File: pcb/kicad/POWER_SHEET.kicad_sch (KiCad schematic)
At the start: 11 parts, among them J1 USB_B_Micro, U1 LMS1585AIS-3.3

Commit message: Update parts/mpns/descriptions etc.
- Incorrect LED part, was 0805 package instead of 0603
- Added MPNs for other parts (mostly ones I already own multiples of)
- Update schematics?
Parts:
- D1: footprint Diode_SMD:Nexperia_DSN1608-2_1.6x0.8mm -> Diode_SMD:D_SOD-523; MPN (none) -> PESD5V0X1UAB,115
- J1: MPN (none) -> 10118194-0001LF
- R1: MPN (none) -> RT0603DRE071KL
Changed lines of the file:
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@@
+			)
+		)
+		(property "MPN" "10118194-0001LF"
+			(at 68.58 72.39 90)
+			(effects
+				(font
+					(size 1.27 1.27)
+				)
+				(hide yes)
 			)
 		)
@@
 			)
 		)
+		(property "MPN" "RT0603DRE071KL"
+			(at 190.5 62.23 0)
+			(effects
+				(font
+					(size 1.27 1.27)
+				)
+				(hide yes)
+			)
+		)
 		(pin "2"
 		)
@@
 			)
 		)
-		(property "Footprint" "Diode_SMD:Nexperia_DSN1608-2_1.6x0.8mm"
+		(property "Footprint" "Diode_SMD:D_SOD-523"
 			(at 48.895 63.5 0)
 			(effects
@@
 			)
 		)
-		(property "Datasheet" "https://assets.nexperia.com/documents/data-sheet/PTVS5V0Z1USKP.pdf"
+		(property "Datasheet" ""
 			(at 53.34 63.5 0)
 			(effects
@@
 			)
 		)
-		(property "Description" "5V, 2000W TVS unidirectional diode, DSN1608-2"
+		(property "Description" "5V, TVS unidirectional diode"
 			(at 53.34 63.5 0)
 			(effects
 				(font
+					(size 1.27 1.27)
+				)
+				(hide yes)
+			)
+		)
+		(property "MPN" "PESD5V0X1UAB,115"
+			(at 53.34 63.5 90)
+			(effects
+				(font

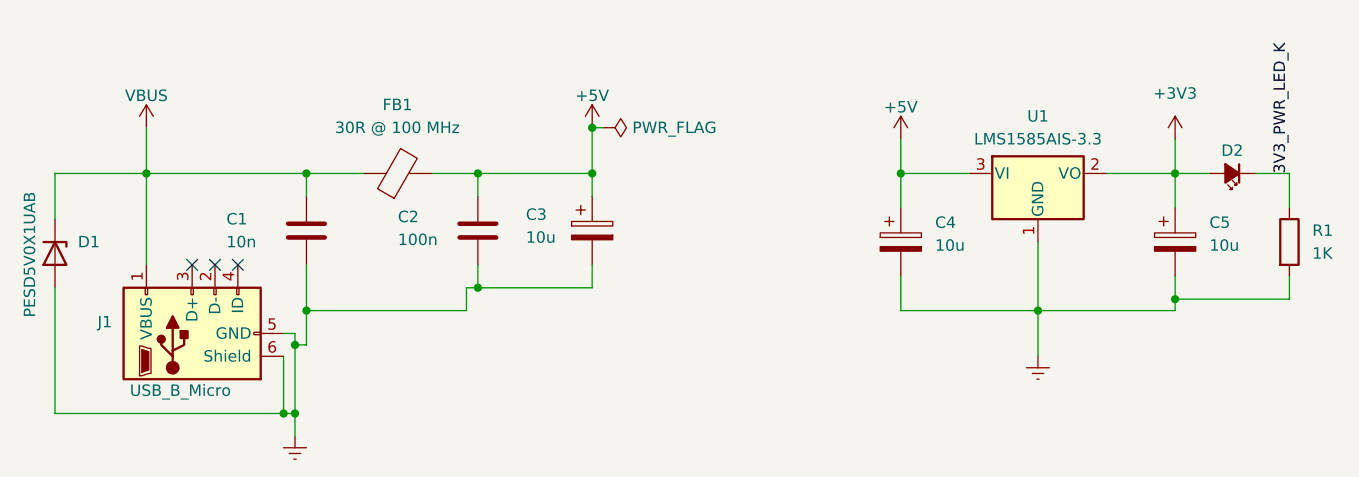
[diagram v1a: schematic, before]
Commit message: Remove additional input cap on ldo
- Already an input capacitor due to the pi-filter on the VBUS line,
  therefore another input capacitor isn't needed
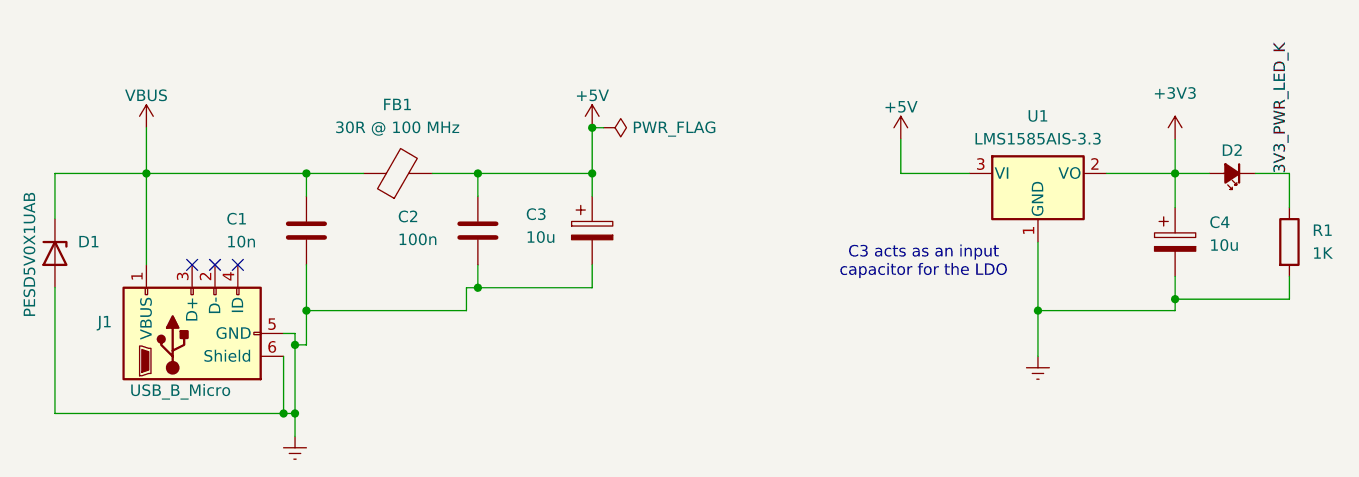
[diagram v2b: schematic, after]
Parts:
- removed C4: 10u, Capacitor_SMD:CP_Elec_4x4.5, symbol Device:C_Polarized
- renumbered C5 to C4
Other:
- note added: "C3 acts as an input capacitor for the LDO"
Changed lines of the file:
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@@
 	(title_block
 		(title "Power Sheet")
-		(date "2025-05-06")
-		(rev "v06")
+		(date "2025-05-21")
+		(rev "v07")
 		(comment 4 "All things power related")
+	)
+	(text "C3 acts as an input \ncapacitor for the LDO"
+		(exclude_from_sim no)
+		(at 149.86 64.516 0)
+		(effects
+			(font
+				(size 1.27 1.27)
+			)
+		)
 	)
 	(junction
@@
 	)
 	(junction
-		(at 147.32 54.61)
-		(diameter 0)
-		(color 0 0 0 0)
-	)
-	(junction
 		(at 80.01 73.66)
 		(diameter 0)
@@
 	(wire
 		(pts
-			(xy 147.32 54.61) (xy 147.32 58.42)
-		)
-		(stroke
-			(width 0)
-			(type default)
-		)
-	)
-	(wire
-		(pts
 			(xy 177.8 66.04) (xy 177.8 68.58)
 		)
@@
 	(wire
 		(pts
-			(xy 147.32 69.85) (xy 162.56 69.85)
-		)
-		(stroke
-			(width 0)
-			(type default)
-		)
-	)
-	(wire
-		(pts
 			(xy 100.33 67.31) (xy 113.03 67.31)
 		)
@@
 		(pts
 			(xy 99.06 69.85) (xy 81.28 69.85)
-		)
-		(stroke
-			(width 0)
-			(type default)
-		)
-	)
-	(wire
-		(pts
-			(xy 147.32 66.04) (xy 147.32 69.85)
 		)
 		(stroke
@@
 		(dnp no)
 		(fields_autoplaced yes)
-		(property "Reference" "C5"
+		(property "Reference" "C4"
 			(at 181.61 60.0709 0)
 			(effects
@@
 			(project "i2s_spekky_matrix"
 				(path "/e164be4c-4870-49b4-a08f-d162a756edc1/8084362c-1e50-4cdc-88cb-8f42b053a44a"
-					(reference "C5")
+					(reference "C4")
 					(unit 1)
 				)
@@
 					(unit 1)
 				)
-			)
-		)
-	)
-	(symbol
-		(lib_id "Device:C_Polarized")
-		(at 147.32 62.23 0)
-		(unit 1)
-		(exclude_from_sim no)
-		(in_bom yes)
-		(on_board yes)
-		(dnp no)
-		(fields_autoplaced yes)
-		(property "Reference" "C4"
-			(at 151.13 60.0709 0)
-			(effects
-				(font
-					(size 1.27 1.27)
-				)
-				(justify left)
-			)
-		)
-		(property "Value" "10u"
-			(at 151.13 62.6109 0)
-			(effects
-				(font
-					(size 1.27 1.27)
-				)
-				(justify left)
-			)
-		)
-		(property "Footprint" "Capacitor_SMD:CP_Elec_4x4.5"
-			(at 148.2852 66.04 0)
-			(effects
-				(font
-					(size 1.27 1.27)
-				)
-				(hide yes)
-			)
-		)
-		(property "Datasheet" "~"
-			(at 147.32 62.23 0)
-			(effects
-				(font
-					(size 1.27 1.27)
-				)
-				(hide yes)
-			)
-		)
-		(property "Description" "Polarized capacitor"
-			(at 147.32 62.23 0)
-			(effects
-				(font
-					(size 1.27 1.27)
-				)
-				(hide yes)
-			)
-		)
-		(pin "1"
-		)
-		(pin "2"
-		)
-		(instances
-			(project "i2s_spekky_matrix"
-				(path "/e164be4c-4870-49b4-a08f-d162a756edc1/8084362c-1e50-4cdc-88cb-8f42b053a44a"
-					(reference "C4")
-					(unit 1)
-				)
